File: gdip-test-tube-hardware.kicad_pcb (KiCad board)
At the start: 2 copper layers, 76.2 x 58.5 mm, 75 parts, among them J1 USB_B, J2 USB_B, J3 Screw_Terminal_01x02, J4 Conn_01x04, J5 Conn_01x03, J6 Screw_Terminal_01x02, J7 Conn_01x02, Q1 BC818, Q2 BC818, Q3 BC818, SW1 SW_Push, SW2 SW_Push, U1 ESP32-S3-WROOM-1-N16R2, U2 AMS1117-3.3, U3 CP2102N-Axx-xQFN28, U4 USBLC6-2SC6, U5 USBLC6-2SC6, U6 74LVC2G00, U7 HDSP-7401, U8 74AHC595, U9 TPS22810DBVT

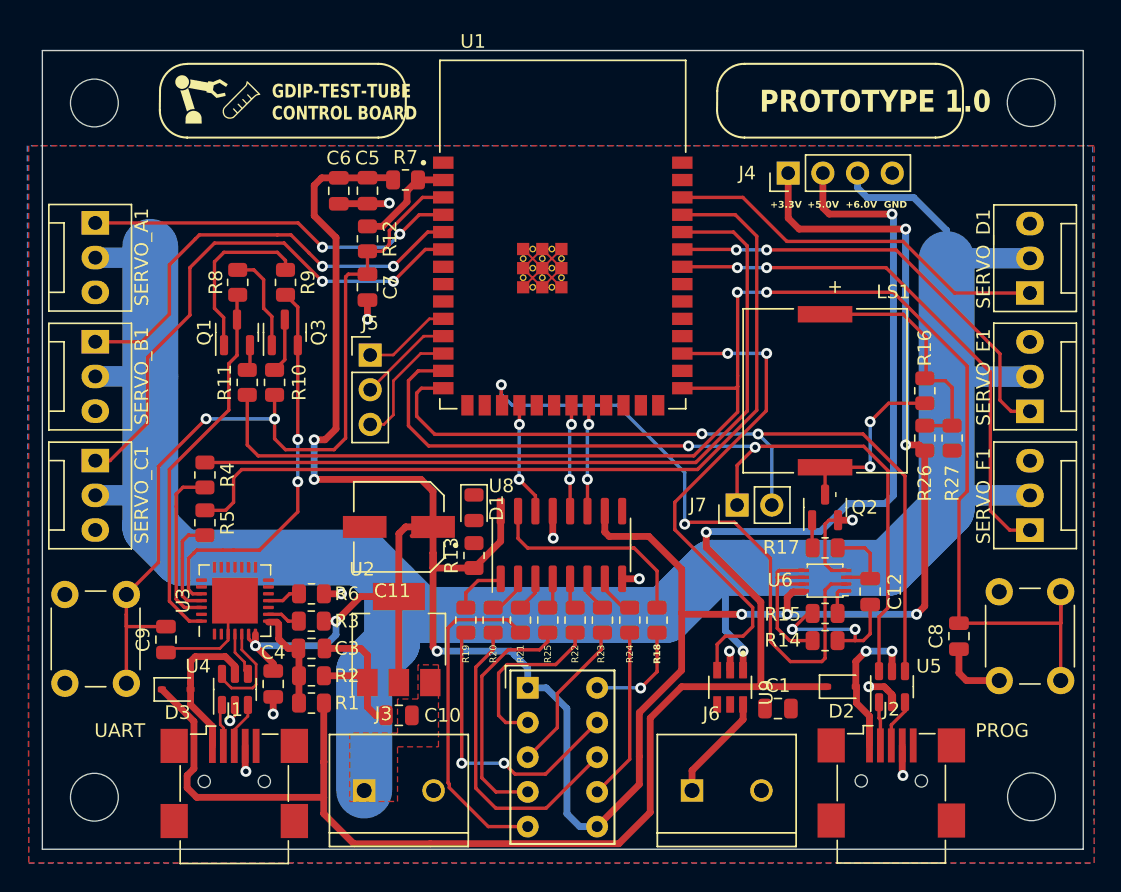
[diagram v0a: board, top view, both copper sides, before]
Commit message: Moved PWR led and added a DEBUG led in better locations. Also tested the step file of a molex part for servro headers.
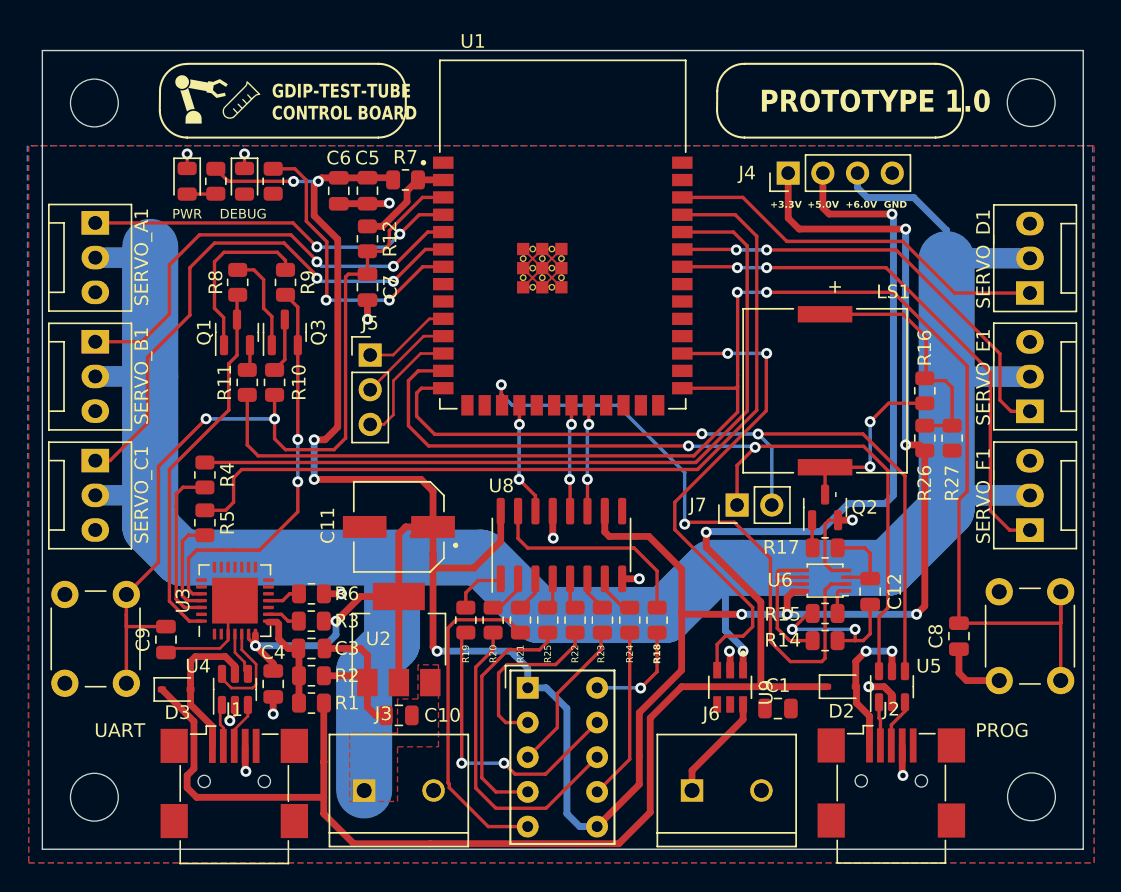
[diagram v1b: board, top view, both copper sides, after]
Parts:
- added DEBUG: LED, LED_SMD:LED_0805_2012Metric, F.Cu at (114.8, 89.1)
- added R28: 330, Resistor_SMD:R_0805_2012Metric, F.Cu at (116.9, 89.1)
- PWR: renamed from D1; value MCUPWR -> LED
- moved R13 33.3 mm to (112.7, 89.1), turned to -90 degrees
- moved PWR 31.8 mm to (110.6, 89.1)
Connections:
- U1 pad 7: unconnected-(U1-IO7-Pad7) -> /GPIO_LED
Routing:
- net /GPIO_LED: track 0.00 -> 21.8 mm, vias 0 -> 2
- net +3.3V: track 206.1 -> 214.1 mm, vias 10 -> 12
- net GND: track 68.0 -> 70.1 mm, vias 12 -> 14
- net Net-(PWR1-A): track 0.00 -> 2.11 mm

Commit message: Reviewed schematic and made changes please view docs folder for more info. Schematic now complete.
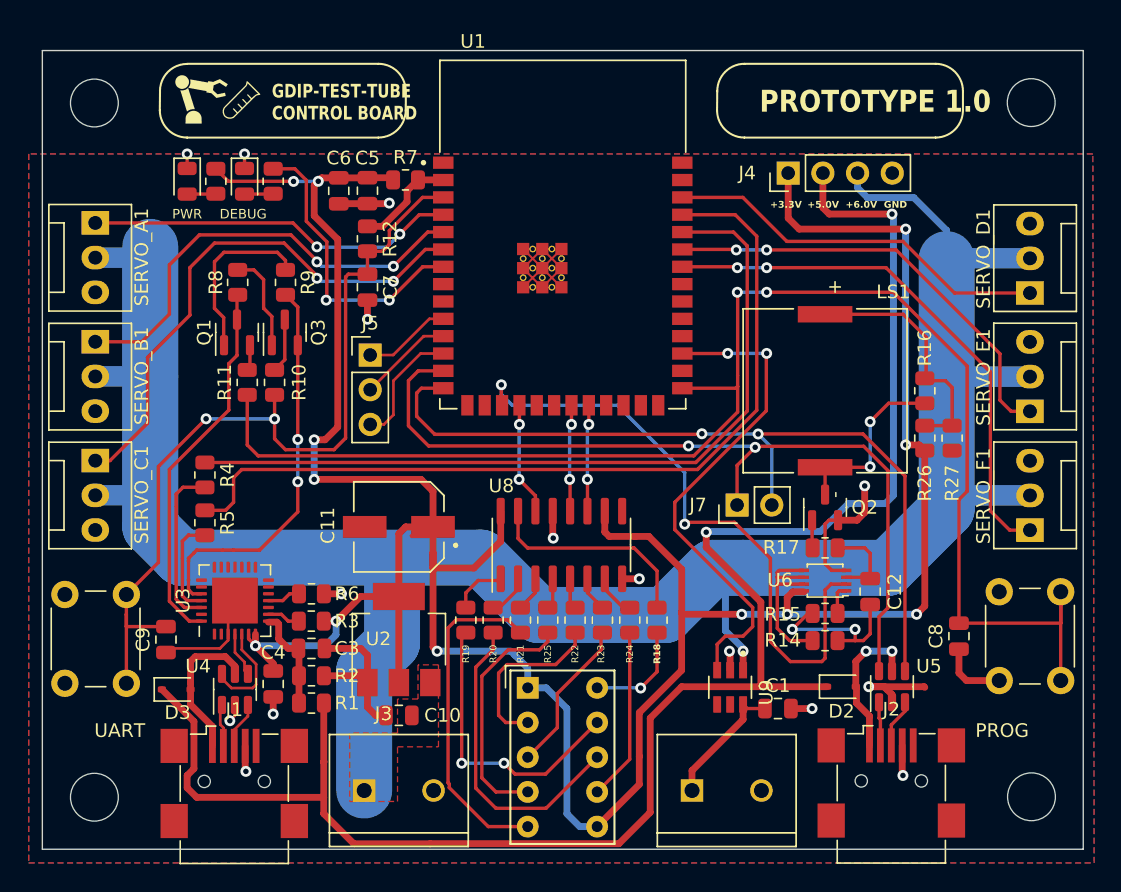
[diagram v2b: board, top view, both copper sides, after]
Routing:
- net GND: track 70.1 -> 78.8 mm, vias 14 -> 15
- net Net-(DEBUG1-A): track 0.00 -> 2.11 mm
- net Net-(J6-Pin_1): track 7.85 -> 9.57 mm

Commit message: Inital DRC check all complete, now doing final run over.
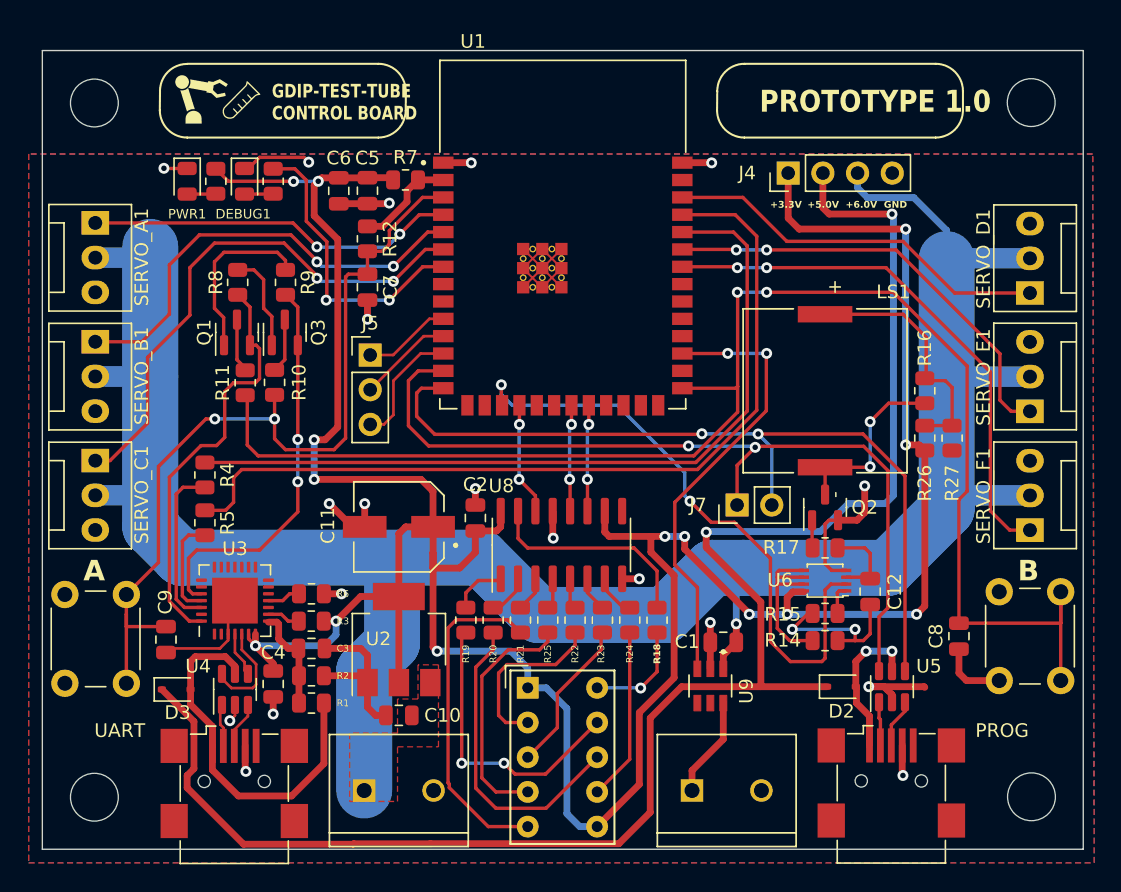
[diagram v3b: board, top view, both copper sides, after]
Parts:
- added C2: 10uF, Capacitor_SMD:C_0805_2012Metric, F.Cu at (131.7, 113.8)
- C5: value 10uF -> 0.1uF
- C6: value 0.1uF -> 10uF
- C7: value 100nF -> 1uF
- moved C1 6.29 mm to (149.8, 122.8), turned to 180 degrees
- moved U9 1.45 mm to (148.9, 126.0)
- moved R11 0.15 mm to (114.8, 103.8)
- renumbered DEBUG to DEBUG1, PWR to PWR1
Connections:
- C1 pad 1: Net-(J6-Pin_1) -> +6V
- D3 pad 2: Net-(D3-A) -> VBUS
- J1 pad 1: Net-(D3-A) -> VBUS
- Q1 pad 2: Net-(Q1-E) -> /DTR
- Q1 pad 3: /DTR -> Net-(Q1-C)
- R1 pad 1: +5V -> VBUS
- R11 pad 2: Net-(Q1-E) -> Net-(Q1-C)
- U4 pad 5: Net-(D3-A) -> VBUS
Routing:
- net VBUS: track 0.00 -> 27.2 mm
- net GND: track 78.8 -> 94.4 mm, vias 15 -> 19
- net Net-(D3-A): track 11.1 -> 0.00 mm
- net +5V: track 129.6 -> 122.0 mm
- net Net-(Q1-C): track 0.00 -> 4.00 mm
- net /GPIO_LED_SWITCH: track 36.4 -> 32.8 mm
- net +3.3V: track 214.1 -> 217.6 mm, vias 12 -> 14
- net /DTR: track 27.5 -> 30.6 mm
- net Net-(J6-Pin_1): track 9.57 -> 7.35 mm
- net Net-(Q1-E): track 1.90 -> 0.00 mm
- net /PWM6: track 46.8 -> 45.4 mm
- net +6V: track 169.6 -> 169.0 mm
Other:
- board text added: "+"
- board text added: "-"
- board text added: "A"
- board text added: "B"
- board text added: "MOTOR POWER (6V)"
- board text added: "WARNING LEDS (5V)"
